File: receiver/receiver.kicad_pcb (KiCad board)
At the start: 2 copper layers, 71.4 x 53.5 mm, 42 parts, among them CON1 AVR-ISP-6, IC1 ATTINY441-SSU, P1 LASER, P2 BATTERY, P3 CONN_01X01, P4 CONN_01X01, Q1 OPTO_NPN, Q2 OPTO_NPN, Q3 OPTO_NPN, Q4 OPTO_NPN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

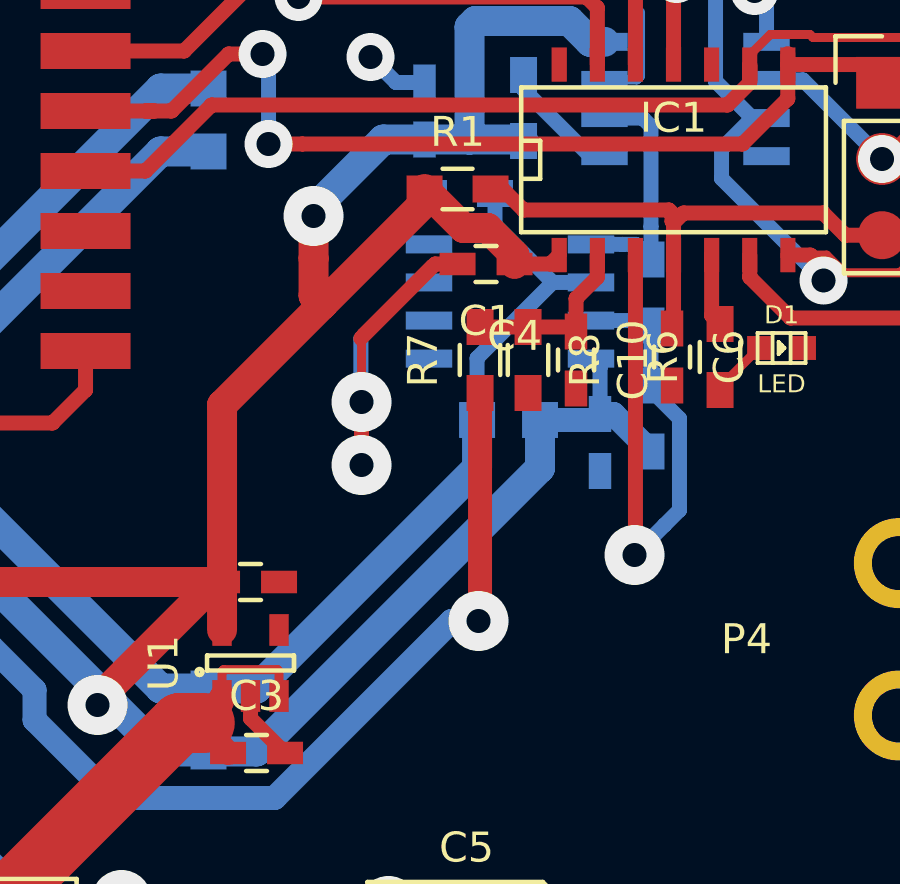
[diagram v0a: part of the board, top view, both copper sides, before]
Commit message: Swap comparator pins on PCB, move R5 so that ground connection is shorter
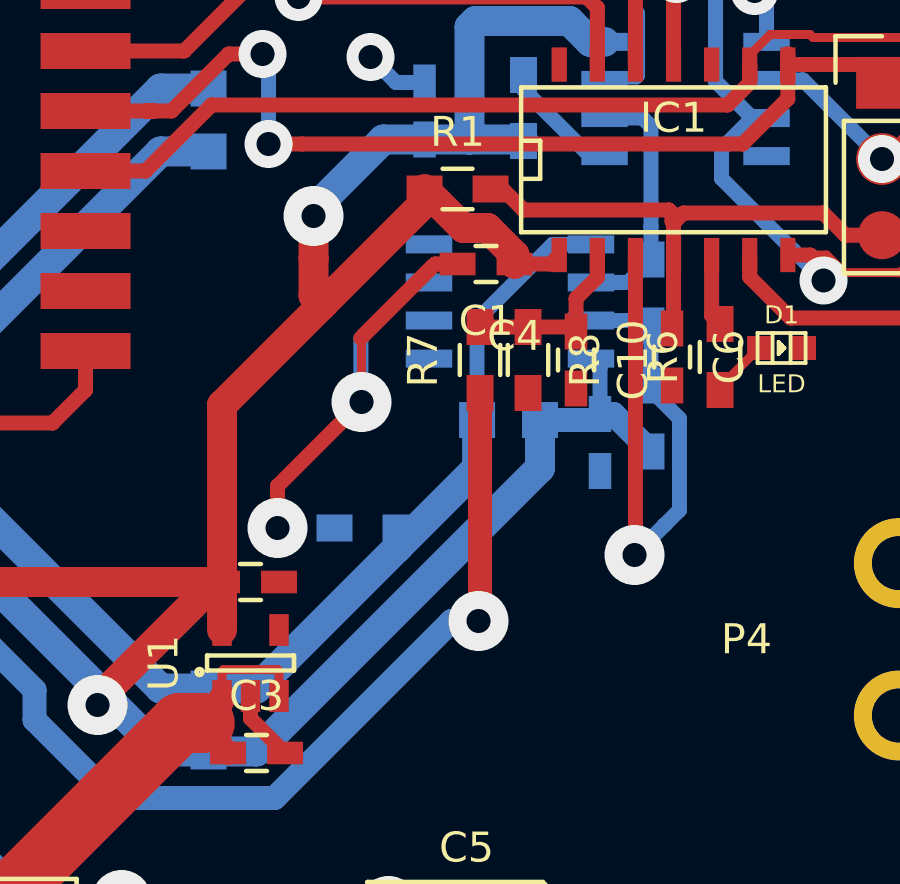
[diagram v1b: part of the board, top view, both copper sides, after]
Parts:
- moved R5 11.6 mm to (92.5, 109.5)
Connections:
- CON1 pad 2: (no net) -> Net-(CON1-Pad2)
- IC1 pad 10: (no net) -> Net-(IC1-Pad10)
- U2 pad 5: /THRESHOLD -> /MATRIX_OUT
- U2 pad 6: /MATRIX_OUT -> /THRESHOLD
- U4 pad 1: (no net) -> Net-(U4-Pad1)
- U4 pad 10: (no net) -> Net-(U4-Pad10)
- U4 pad 16: (no net) -> Net-(U4-Pad16)
- U4 pad 3: (no net) -> Net-(U4-Pad3)
- U4 pad 4: (no net) -> Net-(U4-Pad4)
- U4 pad 5: (no net) -> Net-(U4-Pad5)
- U4 pad 6: (no net) -> Net-(U4-Pad6)
- U4 pad 7: (no net) -> Net-(U4-Pad7)
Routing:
- net GND: track 74.9 -> 78.2 mm
- net /MATRIX_OUT: track 51.8 -> 49.7 mm
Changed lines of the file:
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@@
     (links 92)
     (no_connects 0)
-    (area 44.881429 80 133.85 143.700001)
+    (area 51.439999 80.438651 122.974692 134.024753)
     (thickness 1.6)
     (drawings 469)
-    (tracks 340)
+    (tracks 338)
     (zones 0)
     (modules 42)
-    (nets 22)
+    (nets 32)
   )
   (page A4)
@@
   )
   (setup
-    (last_trace_width 0.3)
+    (last_trace_width 0.5)
     (user_trace_width 0.3)
     (user_trace_width 0.5)
@@
   (net 20 /LASER_ON)
   (net 21 /DIGIPOT_SELECT)
+  (net 22 "Net-(CON1-Pad2)")
+  (net 23 "Net-(IC1-Pad10)")
+  (net 24 "Net-(U4-Pad1)")
+  (net 25 "Net-(U4-Pad3)")
+  (net 26 "Net-(U4-Pad4)")
+  (net 27 "Net-(U4-Pad5)")
+  (net 28 "Net-(U4-Pad6)")
+  (net 29 "Net-(U4-Pad7)")
+  (net 30 "Net-(U4-Pad10)")
+  (net 31 "Net-(U4-Pad16)")
   (net_class Default "This is the default net class."
     (clearance 0.2)
@@
     (add_net /THRESHOLD)
     (add_net GND)
+    (add_net "Net-(CON1-Pad2)")
     (add_net "Net-(D1-Pad1)")
+    (add_net "Net-(IC1-Pad10)")
     (add_net "Net-(P1-Pad1)")
     (add_net "Net-(Q5-Pad1)")
     (add_net "Net-(R4-Pad2)")
+    (add_net "Net-(U4-Pad1)")
+    (add_net "Net-(U4-Pad10)")
+    (add_net "Net-(U4-Pad16)")
+    (add_net "Net-(U4-Pad3)")
+    (add_net "Net-(U4-Pad4)")
+    (add_net "Net-(U4-Pad5)")
+    (add_net "Net-(U4-Pad6)")
+    (add_net "Net-(U4-Pad7)")
     (add_net VAA)
     (add_net VCC)
@@
     (pad 1 smd rect (at 0 0) (size 1.7272 1.7272) (layers F.Cu F.Paste F.Mask)
       (net 17 /MISO))
-    (pad 2 smd oval (at 2.54 0) (size 1.7272 1.7272) (layers F.Cu F.Paste F.Mask))
+    (pad 2 smd oval (at 2.54 0) (size 1.7272 1.7272) (layers F.Cu F.Paste F.Mask)
+      (net 22 "Net-(CON1-Pad2)"))
     (pad 3 smd oval (at 0 2.54) (size 1.7272 1.7272) (layers F.Cu F.Paste F.Mask)
       (net 18 /SCK))
@@
     (pad 14 smd rect (at -3.81 -3.048) (size 0.508 1.143) (layers F.Cu F.Paste F.Mask)
       (net 2 GND))
-    (pad 10 smd rect (at 1.27 -3.048) (size 0.508 1.143) (layers F.Cu F.Paste F.Mask))
+    (pad 10 smd rect (at 1.27 -3.048) (size 0.508 1.143) (layers F.Cu F.Paste F.Mask)
+      (net 23 "Net-(IC1-Pad10)"))
     (model SMD_Packages.3dshapes/SOIC-14_N.wrl
       (at (xyz 0 0 0))
@@
   )
   (module Resistors_SMD:R_0603_HandSoldering (layer B.Cu)
-    (at 95.648026 98.35 180)
+    (at 92.5 109.5 180)
     (descr "Resistor SMD 0603, hand soldering")
     (tags "resistor 0603")
@@
       (net 2 GND))
     (pad 5 smd rect (at 2.7 -1.905) (size 1.55 0.6) (layers B.Cu B.Paste B.Mask)
+      (net 14 /MATRIX_OUT))
+    (pad 6 smd rect (at 2.7 -0.635) (size 1.55 0.6) (layers B.Cu B.Paste B.Mask)
       (net 16 /THRESHOLD))
-    (pad 6 smd rect (at 2.7 -0.635) (size 1.55 0.6) (layers B.Cu B.Paste B.Mask)
-      (net 14 /MATRIX_OUT))
     (pad 7 smd rect (at 2.7 0.635) (size 1.55 0.6) (layers B.Cu B.Paste B.Mask)
       (net 8 /LASER_DETECT))
@@
     (fp_line (start -3.4 15) (end 20.3 15) (layer B.CrtYd) (width 0.15))
     (fp_line (start -3.4 -1) (end 20.3 -1) (layer B.CrtYd) (width 0.15))
-    (pad 1 smd rect (at -1.4 0) (size 3 1.2) (layers F.Cu F.Paste F.Mask))
+    (pad 1 smd rect (at -1.4 0) (size 3 1.2) (layers F.Cu F.Paste F.Mask)
+      (net 24 "Net-(U4-Pad1)"))
     (pad 2 smd rect (at -1.4 2) (size 3 1.2) (layers F.Cu F.Paste F.Mask)
       (net 10 /INT))
-    (pad 3 smd rect (at -1.4 4) (size 3 1.2) (layers F.Cu F.Paste F.Mask))
-    (pad 4 smd rect (at -1.4 6) (size 3 1.2) (layers F.Cu F.Paste F.Mask))
-    (pad 5 smd rect (at -1.4 8) (size 3 1.2) (layers F.Cu F.Paste F.Mask))
-    (pad 6 smd rect (at -1.4 10) (size 3 1.2) (layers F.Cu F.Paste F.Mask))
-    (pad 7 smd rect (at -1.4 12) (size 3 1.2) (layers F.Cu F.Paste F.Mask))
+    (pad 3 smd rect (at -1.4 4) (size 3 1.2) (layers F.Cu F.Paste F.Mask)
+      (net 25 "Net-(U4-Pad3)"))
+    (pad 4 smd rect (at -1.4 6) (size 3 1.2) (layers F.Cu F.Paste F.Mask)
+      (net 26 "Net-(U4-Pad4)"))
+    (pad 5 smd rect (at -1.4 8) (size 3 1.2) (layers F.Cu F.Paste F.Mask)
+      (net 27 "Net-(U4-Pad5)"))
+    (pad 6 smd rect (at -1.4 10) (size 3 1.2) (layers F.Cu F.Paste F.Mask)
+      (net 28 "Net-(U4-Pad6)"))
+    (pad 7 smd rect (at -1.4 12) (size 3 1.2) (layers F.Cu F.Paste F.Mask)
+      (net 29 "Net-(U4-Pad7)"))
     (pad 8 smd rect (at -1.4 14) (size 3 1.2) (layers F.Cu F.Paste F.Mask)
       (net 1 VCC))
     (pad 9 smd rect (at 18.3 14) (size 3 1.2) (layers F.Cu F.Paste F.Mask)
       (net 2 GND))
-    (pad 10 smd rect (at 18.3 12) (size 3 1.2) (layers F.Cu F.Paste F.Mask))
+    (pad 10 smd rect (at 18.3 12) (size 3 1.2) (layers F.Cu F.Paste F.Mask)
+      (net 30 "Net-(U4-Pad10)"))
     (pad 11 smd rect (at 18.3 10) (size 3 1.2) (layers F.Cu F.Paste F.Mask)
       (net 2 GND))
@@
     (pad 15 smd rect (at 18.3 2) (size 3 1.2) (layers F.Cu F.Paste F.Mask)
       (net 11 /RADIO_SELECT))
-    (pad 16 smd rect (at 18.3 0) (size 3 1.2) (layers F.Cu F.Paste F.Mask))
+    (pad 16 smd rect (at 18.3 0) (size 3 1.2) (layers F.Cu F.Paste F.Mask)
+      (net 31 "Net-(U4-Pad16)"))
     (model mysensors.3dshapes/rfm69hw.wrl
       (at (xyz 0.332 -0.275 0.03))
@@
   (segment (start 98.24902 107.49944) (end 88.79944 116.94902) (width 1) (layer B.Cu) (net 1))
   (segment (start 88.79944 116.94902) (end 87.2 116.94902) (width 1) (layer B.Cu) (net 1))
+  (segment (start 89.5 108.1) (end 89.5 109.499996) (width 0.5) (layer F.Cu) (net 2))
+  (segment (start 92.3 105.3) (end 89.5 108.1) (width 0.5) (layer F.Cu) (net 2))
+  (via (at 89.5 109.499996) (size 2) (drill 0.8) (layers F.Cu B.Cu) (net 2))
   (segment (start 112.19 101.23999) (end 112.2 101.24999) (width 0.3) (layer F.Cu) (net 2))
   (via (at 112.2 101.24999) (size 1.6) (drill 0.8) (layers F.Cu B.Cu) (net 2))
@@
   (segment (start 85.8 124.5) (end 85.9 124.4) (width 0.5) (layer F.Cu) (net 2))
   (via (at 85.9 124.4) (size 2) (drill 0.8) (layers F.Cu B.Cu) (net 2))
-  (segment (start 92.3 105.3) (end 92.3 107.4) (width 0.5) (layer F.Cu) (net 2))
-  (via (at 92.3 107.4) (size 2) (drill 0.8) (layers F.Cu B.Cu) (net 2))
   (segment (start 92.277082 103.177082) (end 92.277082 105.277082) (width 0.5) (layer B.Cu) (net 2))
   (segment (start 92.277082 105.277082) (end 92.3 105.3) (width 0.5) (layer B.Cu) (net 2))
@@
   (segment (start 56.61 113.2) (end 61.69 113.2) (width 2) (layer F.Cu) (net 13))
   (segment (start 61.69 113.2) (end 64.23 110.66) (width 2) (layer F.Cu) (net 13))
-  (segment (start 96.15098 105.9) (end 96.15098 103.837046) (width 0.5) (layer B.Cu) (net 14))
-  (segment (start 96.15098 103.837046) (end 98.673026 101.315) (width 0.5) (layer B.Cu) (net 14))
-  (segment (start 98.673026 101.315) (end 99.948026 101.315) (width 0.5) (layer B.Cu) (net 14))
-  (segment (start 96.598026 98.35) (end 96.748026 98.35) (width 0.5) (layer B.Cu) (net 14))
-  (segment (start 96.898026 98.35) (end 96.748026 98.35) (width 0.5) (layer B.Cu) (net 14))
+  (segment (start 88.79944 114.85098) (end 93.5 110.15042) (width 1) (layer B.Cu) (net 14))
+  (segment (start 93.5 110.15042) (end 96.15098 107.49944) (width 1) (layer B.Cu) (net 14))
+  (segment (start 93.6 109.5) (end 93.6 110.05042) (width 0.5) (layer B.Cu) (net 14))
+  (segment (start 93.6 110.05042) (end 93.5 110.15042) (width 0.5) (layer B.Cu) (net 14))
+  (segment (start 96.15098 105.9) (end 96.15098 102.567046) (width 0.5) (layer B.Cu) (net 14))
+  (segment (start 96.15098 102.567046) (end 98.673026 100.045) (width 0.5) (layer B.Cu) (net 14))
+  (segment (start 98.673026 100.045) (end 99.948026 100.045) (width 0.5) (layer B.Cu) (net 14))
   (segment (start 87.2 114.85098) (end 88.79944 114.85098) (width 1) (layer B.Cu) (net 14))
-  (segment (start 88.79944 114.85098) (end 96.15098 107.49944) (width 1) (layer B.Cu) (net 14))
   (segment (start 96.15098 107.49944) (end 96.15098 105.9) (width 1) (layer B.Cu) (net 14))
   (segment (start 87.2 96.94902) (end 85.60056 96.94902) (width 1) (layer B.Cu) (net 14))
@@
   (segment (start 85.60056 114.85098) (end 78.24902 107.49944) (width 1) (layer B.Cu) (net 14))
   (segment (start 78.24902 107.49944) (end 78.24902 105.9) (width 1) (layer B.Cu) (net 14))
-  (segment (start 96.748026 98.35) (end 96.748026 99.39) (width 0.5) (layer B.Cu) (net 14))
-  (segment (start 96.748026 99.39) (end 98.673026 101.315) (width 0.5) (layer B.Cu) (net 14))
   (segment (start 115.99886 121.95) (end 116.95 121.95) (width 0.8) (layer F.Cu) (net 15))
   (segment (start 116.95 121.95) (end 118.1 120.8) (width 0.8) (layer F.Cu) (net 15))
   (segment (start 118.1 120.8) (end 118.1 120.3) (width 0.8) (layer F.Cu) (net 15))
+  (segment (start 101.948026 100.55) (end 101.183026 101.315) (width 0.5) (layer B.Cu) (net 16))
+  (segment (start 101.183026 101.315) (end 99.948026 101.315) (width 0.5) (layer B.Cu) (net 16))
   (segment (start 100.4 95.835) (end 101.675 95.835) (width 0.5) (layer B.Cu) (net 16))
   (segment (start 101.675 95.835) (end 101.948026 96.108026) (width 0.5) (layer B.Cu) (net 16))
   (segment (start 101.948026 96.108026) (end 101.948026 99.45) (width 0.5) (layer B.Cu) (net 16))
   (segment (start 101.948026 99.45) (end 101.948026 100.55) (width 0.5) (layer B.Cu) (net 16))
-  (segment (start 99.948026 100.045) (end 101 100.045) (width 0.5) (layer B.Cu) (net 16))
-  (segment (start 101 100.045) (end 101.443026 100.045) (width 0.5) (layer B.Cu) (net 16))
-  (segment (start 99.473026 100.045) (end 99.948026 100.045) (width 0.3) (layer B.Cu) (net 16))
   (segment (start 102.010705 100.487321) (end 101.948026 100.55) (width 0.3) (layer B.Cu) (net 16))
-  (segment (start 101.443026 100.045) (end 101.948026 100.55) (width 0.5) (layer B.Cu) (net 16))
   (segment (start 106.51 94.052) (end 106.51 95.19) (width 0.5) (layer F.Cu) (net 17))
   (segment (start 106.51 95.19) (end 105 96.7) (width 0.5) (layer F.Cu) (net 17))

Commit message: REV2 of the board
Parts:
- added C12: 1u, Capacitors_SMD:C_0603_HandSoldering, F.Cu at (81.0, 115.8)
- added C44: C, Capacitors_SMD:C_0603_HandSoldering, F.Cu at (91.5, 112.4)
- added P5: CONN_01X01, w_pin_strip:pin_socket_1, F.Cu at (104.2, 90.5)
- added R11: 10R, Resistors_SMD:R_0603_HandSoldering, F.Cu at (91.2, 100.6)
- added R12: 10R, Resistors_SMD:R_0603_HandSoldering, F.Cu at (85.0, 112.8)
- added R13: 10k, Resistors_SMD:R_0603_HandSoldering, F.Cu at (87.2, 91.5)
- added R14: 10k, Resistors_SMD:R_0603_HandSoldering, F.Cu at (87.2, 93.5)
- added R15: 10k, Resistors_SMD:R_0603_HandSoldering, F.Cu at (87.2, 95.8)
- added R16: 10k, Resistors_SMD:R_0603_HandSoldering, F.Cu at (87.2, 97.5)
- added R17: 10k, Resistors_SMD:R_0603_HandSoldering, F.Cu at (86.5, 87.5)
- added SW1: Switch_SPDT_x2, OS102011, F.Cu at (79.3, 131.7)
- moved C2 3.00 mm to (76.5, 124.4), turned to 270 degrees
- moved C5 2.14 mm to (97.9, 124.2)
- moved C3 0.95 mm to (87.8, 117.0)
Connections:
- C8 pad 1: VCC -> Net-(C12-Pad2)
- C9 pad 1: VCC -> Net-(C9-Pad1)
- Q1 pad 3: VCC -> Net-(C12-Pad2)
- Q2 pad 3: VCC -> Net-(C12-Pad2)
- Q3 pad 3: VCC -> Net-(C12-Pad2)
- Q4 pad 3: VCC -> Net-(C12-Pad2)
- R2 pad 1: VCC -> Net-(C12-Pad2)
- R4 pad 1: VCC -> Net-(C9-Pad1)
- U1 pad 3: VAA -> Net-(SW1-Pad2)
- U2 pad 8: VCC -> Net-(C12-Pad2)
- U3 pad 8: VCC -> Net-(C9-Pad1)
- U4 pad 12: /SCK -> Net-(R16-Pad1)
- U4 pad 13: /MISO -> Net-(R15-Pad1)
- U4 pad 14: /MOSI -> Net-(R14-Pad1)
- U4 pad 15: /RADIO_SELECT -> Net-(R13-Pad1)
- U4 pad 2: /INT -> Net-(R17-Pad2)
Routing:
- net VCC: track 136.6 -> 56.5 mm, vias 2 -> 0
- net Net-(C12-Pad2): track 0.00 -> 61.1 mm, vias 0 -> 1
- net Net-(SW1-Pad2): track 0.00 -> 26.2 mm, vias 0 -> 4
- net /INT: track 41.8 -> 18.0 mm
- net Net-(R17-Pad2): track 0.00 -> 23.7 mm
- net Net-(C9-Pad1): track 0.00 -> 16.8 mm, vias 0 -> 1
- net /MISO: track 34.9 -> 25.1 mm, vias 2 -> 0
- net /RADIO_SELECT: track 28.7 -> 23.2 mm
- net VAA: track 68.6 -> 73.1 mm
- net Net-(IC1-Pad10): track 0.00 -> 3.65 mm
- net /DIGIPOT_SELECT: track 10.8 -> 14.0 mm
- net Net-(R15-Pad1): track 0.00 -> 3.11 mm
- net Net-(R16-Pad1): track 0.00 -> 3.09 mm
- net Net-(R14-Pad1): track 0.00 -> 3.09 mm
- net Net-(R13-Pad1): track 0.00 -> 3.09 mm
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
